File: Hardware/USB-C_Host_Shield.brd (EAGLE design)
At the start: 53.3 x 59.7 mm, 52 parts, among them J1 USB-C, J2 GPIN, J3 GPOUT, J4 Power Select, U1 ARDUINO_UNO_R3_SHIELDBASIC, U2 LM1117, U3 74HC4050, U5 MAX3421, U6 3.3V/150mA, Y1 12.0mhZ

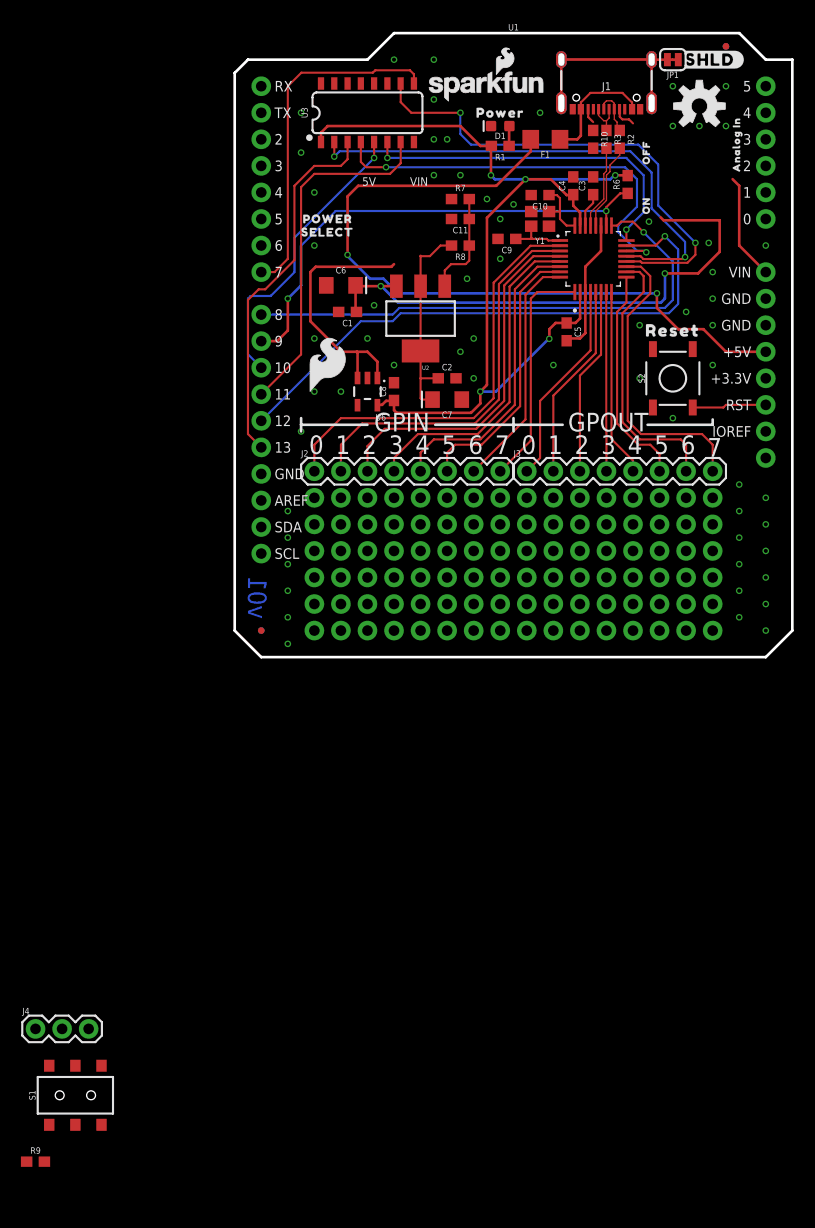
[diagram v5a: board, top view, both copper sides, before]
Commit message: Adjusted schematic with new changes for layout
Changed the main power schema for the USB-C port
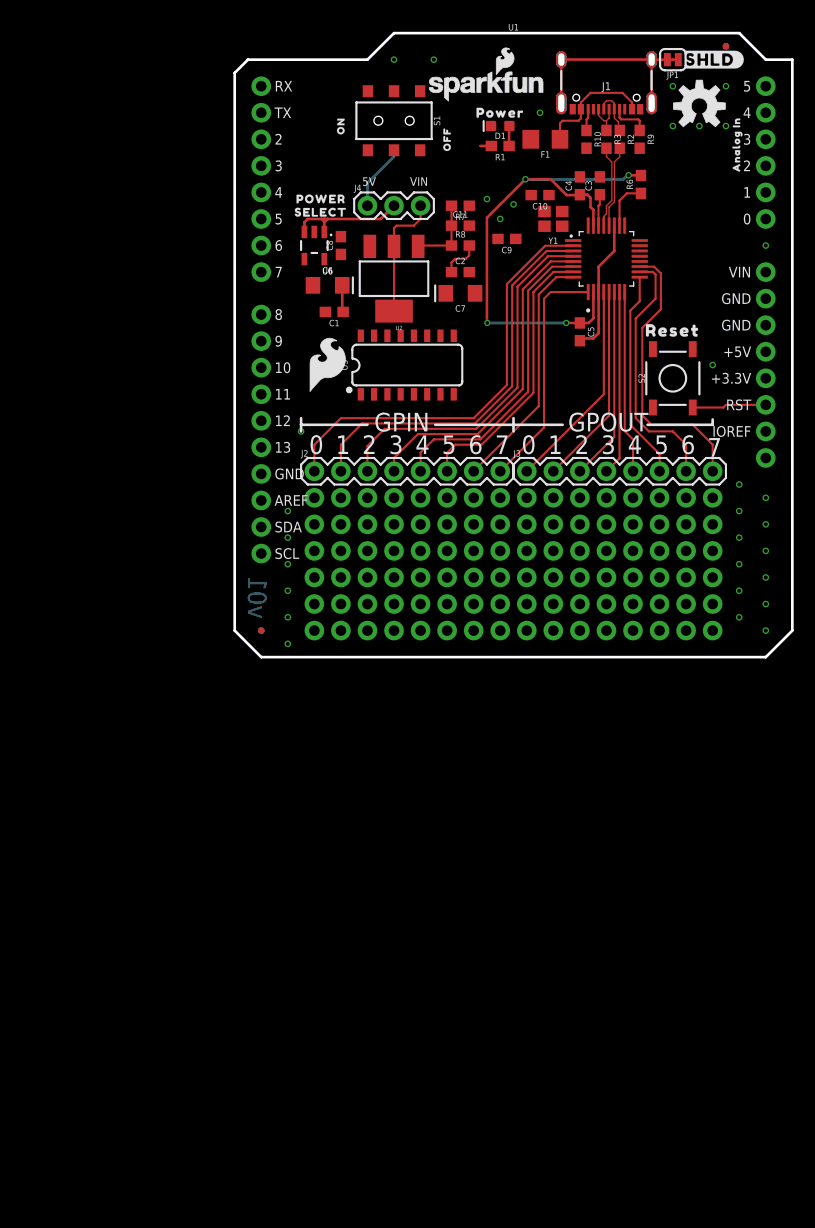
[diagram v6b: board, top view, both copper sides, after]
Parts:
- moved R9 113.6 mm to (38.7, 49.5), turned to 270 degrees
- moved S1 98.1 mm to (15.2, 51.3), turned to 180 degrees
- moved J4 84.9 mm to (12.7, 43.2)
- moved U$5 30.2 mm to (10.2, 50.8)
- moved U3 24.4 mm to (16.5, 27.9)
- moved U$7 19.1 mm to (20.3, 49.5)
- moved C8 14.9 mm to (10.2, 39.4)
- moved U6 14.9 mm to (7.62, 39.4)
- moved C7 10.2 mm to (21.6, 34.8)
- moved C2 10.2 mm to (21.6, 36.8)
- moved U2 4.58 mm to (15.2, 36.2)
- moved U$1 3.81 mm to (36.2, 27.2)
- moved U$12 2.01 mm to (8.26, 43.8)
- moved U$13 2.01 mm to (8.26, 42.5)
- moved C5 1.27 mm to (33.0, 31.1)
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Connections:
- net 5V: no longer F1.2, R10.2, R9.2
- net POWER_IN: now also F1.2, R10.2, R9.2
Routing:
- net 5V: track 70.8 -> 5.75 mm, vias 2 -> 0
- net VIN: track 62.1 -> 2.68 mm, vias 2 -> 0
- net POCI: track 55.6 -> 0.03 mm, vias 1 -> 0
- net GPX: track 51.2 -> 0.00 mm, vias 1 -> 0
- net SCK-IN: track 48.0 -> 0.00 mm, vias 2 -> 0
- net RESET-IN: track 47.2 -> 0.00 mm, vias 2 -> 0
- net 3.3V: track 93.2 -> 50.3 mm, vias 5 -> 4
- net INT: track 46.6 -> 4.73 mm, vias 2 -> 0
- net CS-IN: track 40.3 -> 0.02 mm, vias 2 -> 0
- net SCK: track 35.5 -> 0.00 mm
- net PICO: track 33.9 -> 0.00 mm
- net PICO-IN: track 33.6 -> 0.00 mm, vias 2 -> 0
- net RESET: track 33.3 -> 0.00 mm
- net CS: track 28.2 -> 0.00 mm, vias 1 -> 0
- net POWER_IN: track 25.1 -> 12.3 mm
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
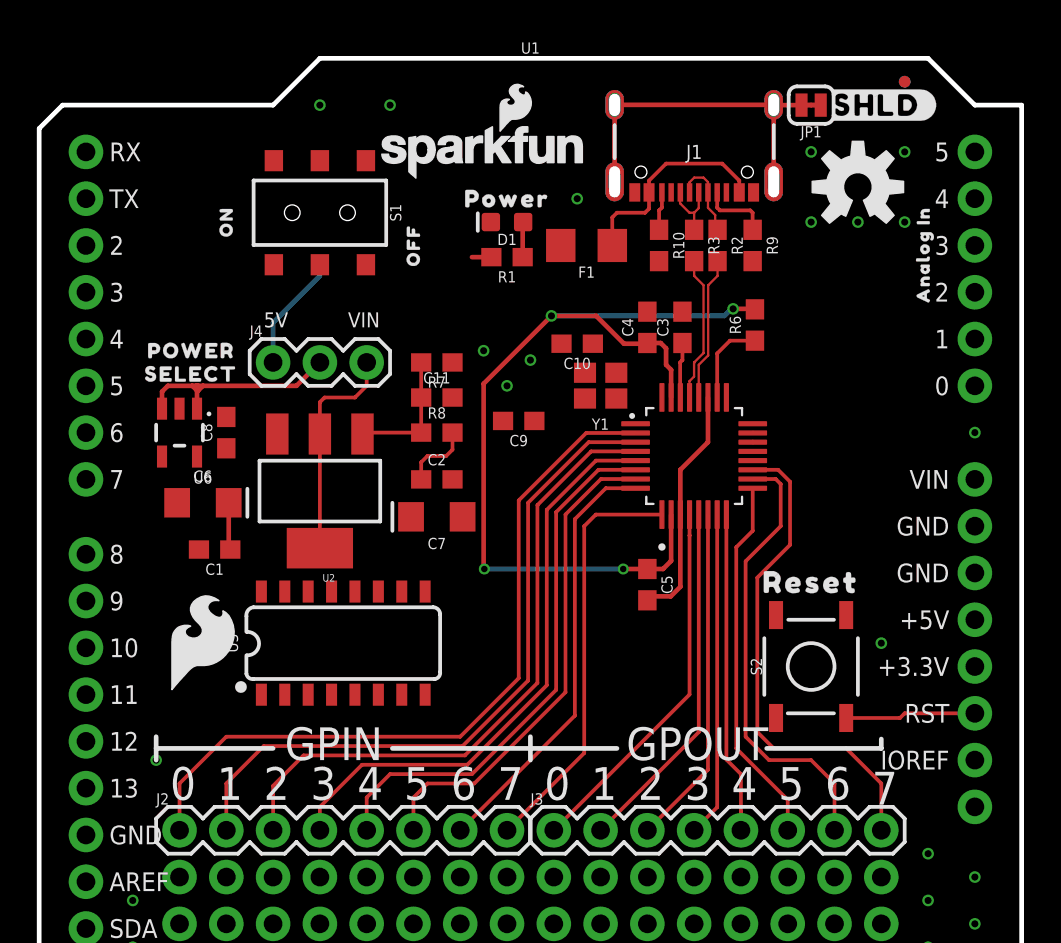
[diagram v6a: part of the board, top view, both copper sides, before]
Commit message: Completed action items
Finished routing after adjusting design to comply with ERC and DRC.
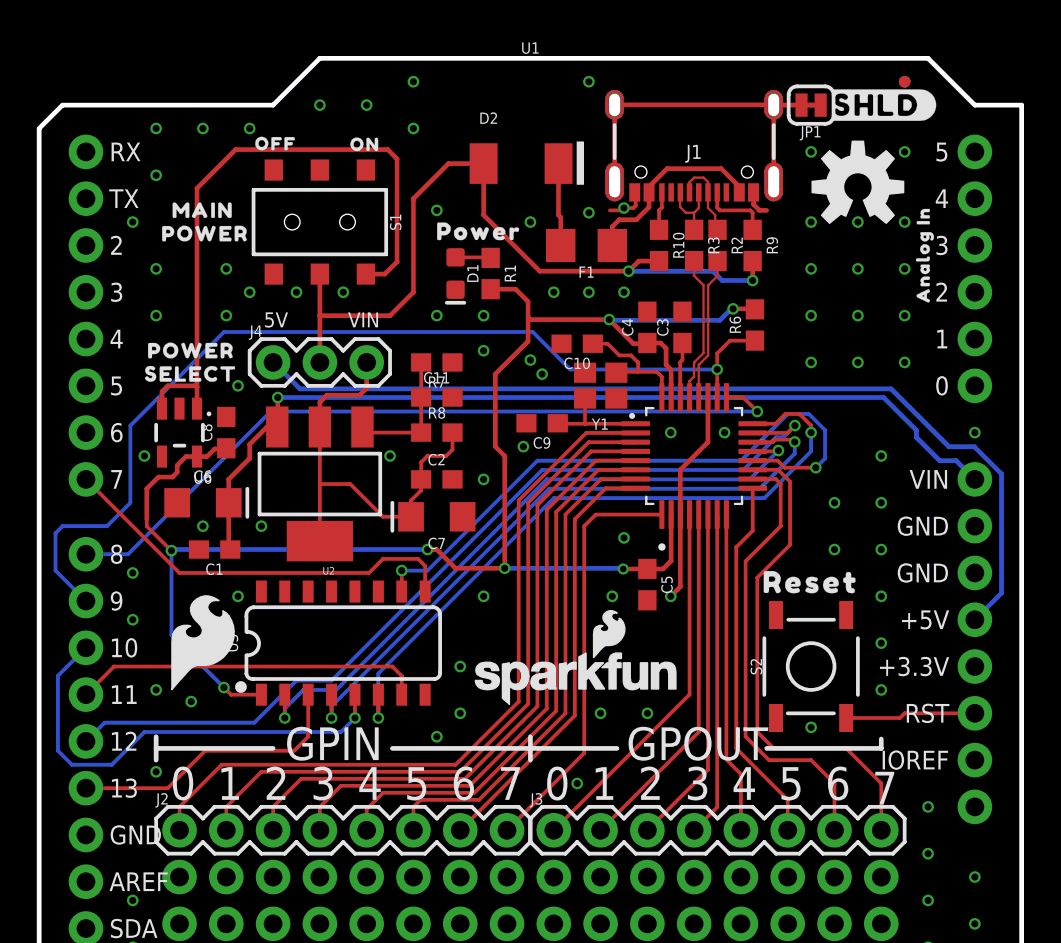
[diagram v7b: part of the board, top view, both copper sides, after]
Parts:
- added D2: 1A/15V/220mV, SparkFun-DiscreteSemi:DO-214BA
- added U$14: (no value), output:POWER38
- added U$15: (no value), output:MAIN40
- S1: value (none) -> Main Power
- moved U$10 29.0 mm to (29.2, 26.0)
- moved U$7 9.29 mm to (12.8, 55.1), turned to 0 degrees
- moved U$5 8.63 mm to (17.7, 55.0), turned to 0 degrees
- moved D1 3.95 mm to (22.6, 48.0), turned to 270 degrees
- moved U$2 2.34 mm to (23.9, 50.3)
- moved C9 1.28 mm to (27.3, 39.9)
- moved R1 1.26 mm to (24.5, 48.0), turned to 270 degrees
- moved S1 0.51 mm to (15.2, 50.8)
- moved U2 0.38 mm to (15.2, 36.6)
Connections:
- removed net N$2: S1.3
- new net N$5: D2.C, F1.2
- new net VDD: D2.A, J4.2, R10.2, R9.2, S1.2
- net GND: now also S1.3
- net POWER_IN: no longer F1.2, J4.2, R10.2, R9.2, S1.2
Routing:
- net INT: track 4.73 -> 52.8 mm, vias 0 -> 1
- net POCI: track 0.03 -> 48.0 mm, vias 0 -> 1
- net VIN: track 2.68 -> 49.6 mm, vias 0 -> 1
- net 5V: track 5.75 -> 50.6 mm
- net VDD: track 0.00 -> 41.9 mm, vias 0 -> 2
- net GPX: track 0.00 -> 41.7 mm, vias 0 -> 1
- net PICO-IN: track 0.00 -> 37.2 mm, vias 0 -> 2
- net 3.3V: track 50.3 -> 87.5 mm, vias 4 -> 7
- net SCK-IN: track 0.00 -> 35.8 mm, vias 0 -> 2
- net CS-IN: track 0.02 -> 35.8 mm, vias 0 -> 2
- net RESET-IN: track 0.00 -> 33.8 mm, vias 0 -> 2
- net CS: track 0.00 -> 25.0 mm, vias 0 -> 1
- net RESET: track 0.00 -> 22.4 mm
- net POWER_IN: track 12.3 -> 34.4 mm
- net PICO: track 0.00 -> 19.0 mm
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
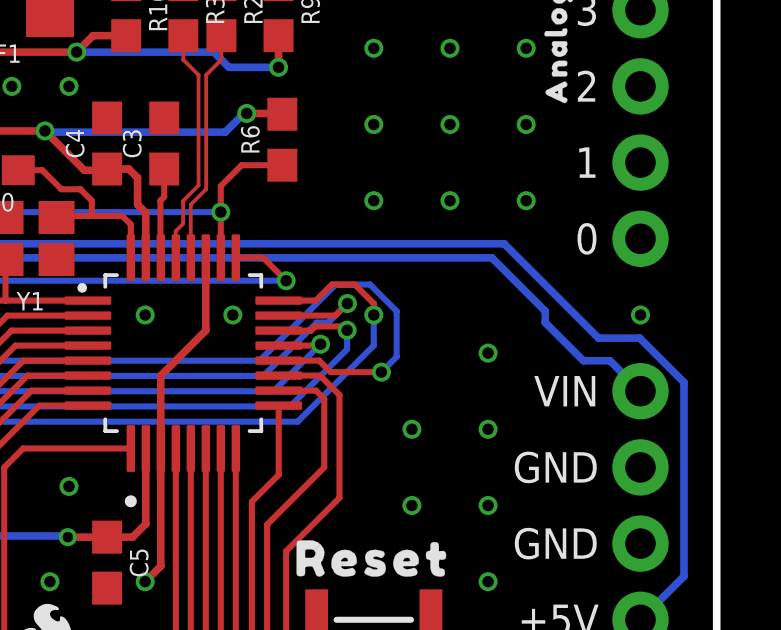
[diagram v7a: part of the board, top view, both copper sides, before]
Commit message: Added more GND vias
More GND vias for better coverage
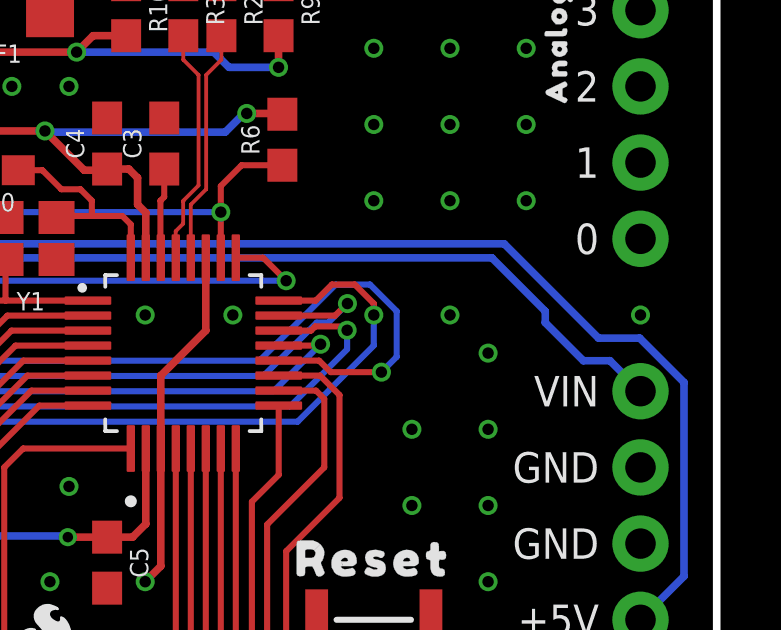
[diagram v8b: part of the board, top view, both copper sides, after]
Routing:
- net GND: vias 97 -> 98
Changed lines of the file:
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@@
 <via x="11.43" y="55.88" extent="1-16" drill="0.381"/>
 <via x="34.29" y="30.48" extent="1-16" drill="0.381"/>
+<via x="44.45" y="39.37" extent="1-16" drill="0.381"/>
 </signal>
 <signal name="N$7">
